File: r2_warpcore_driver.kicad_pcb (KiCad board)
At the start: 4 copper layers, 151 x 94.4 mm, 56 parts, among them J1 Conn_01x04_Pin, J10 Screw_Terminal_01x02, J11 Conn_01x03_Pin, J13 Conn_01x14_Pin, J14 Conn_01x05_Pin, J15 Conn_01x03_Pin, J16 Conn_01x03_Pin, J2 Conn_01x03_Pin, J3 Conn_01x03_Pin, J4 Conn_01x04_Pin, J5 Screw_Terminal_01x04, J6 Conn_01x05_Pin, J7 Screw_Terminal_01x04, J8 Screw_Terminal_01x04, J9 Screw_Terminal_01x03, Q1 L8050QLT1G, Q2 L8050QLT1G, Q3 IRLB8721PBF, Q4 IRLB8721PBF, Q5 IRLB8721PBF, Q6 Q_PNP_BEC, Q7 Q_PNP_BEC, Q8 Q_PNP_BEC, SW1 SW_Push, SW2 SW_Push, U1 ESP32-S3-MINI-1, U2 LDL1117S33R

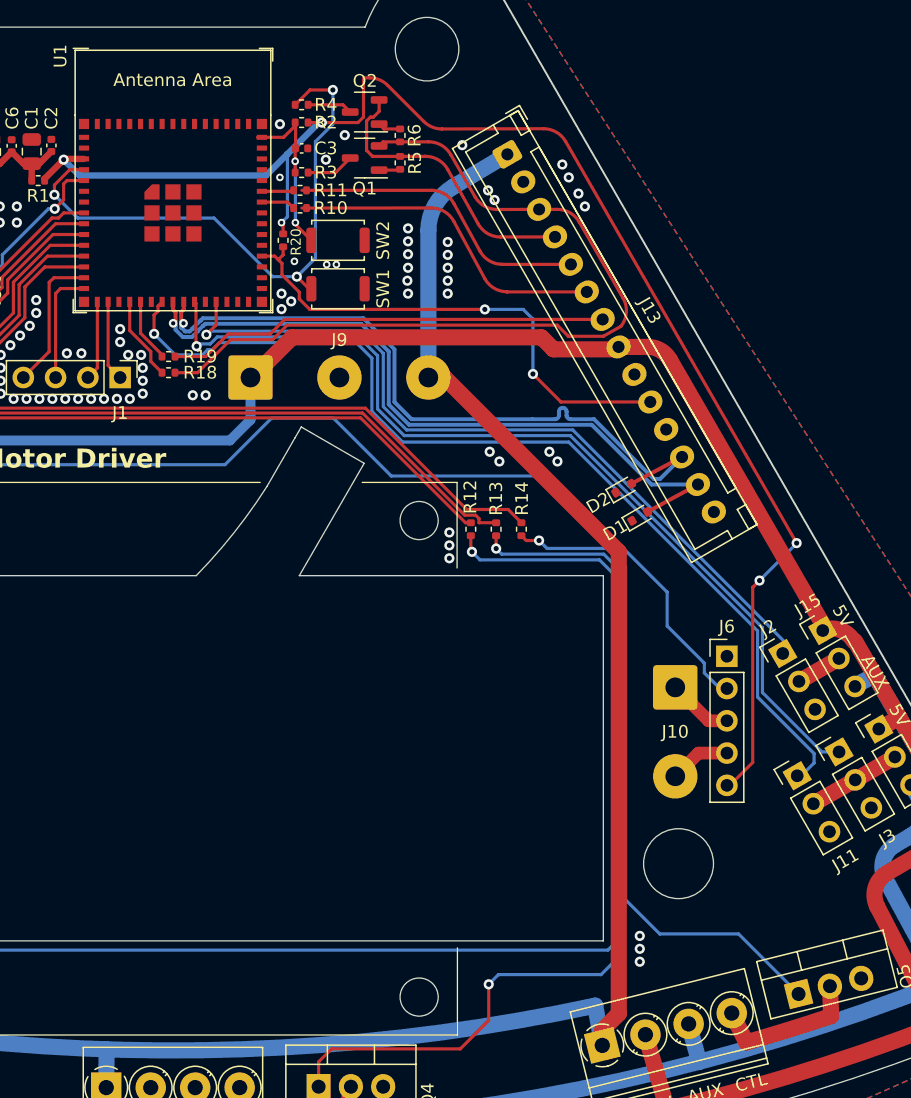
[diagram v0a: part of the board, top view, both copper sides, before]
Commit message: Updates to move to a USB socket.
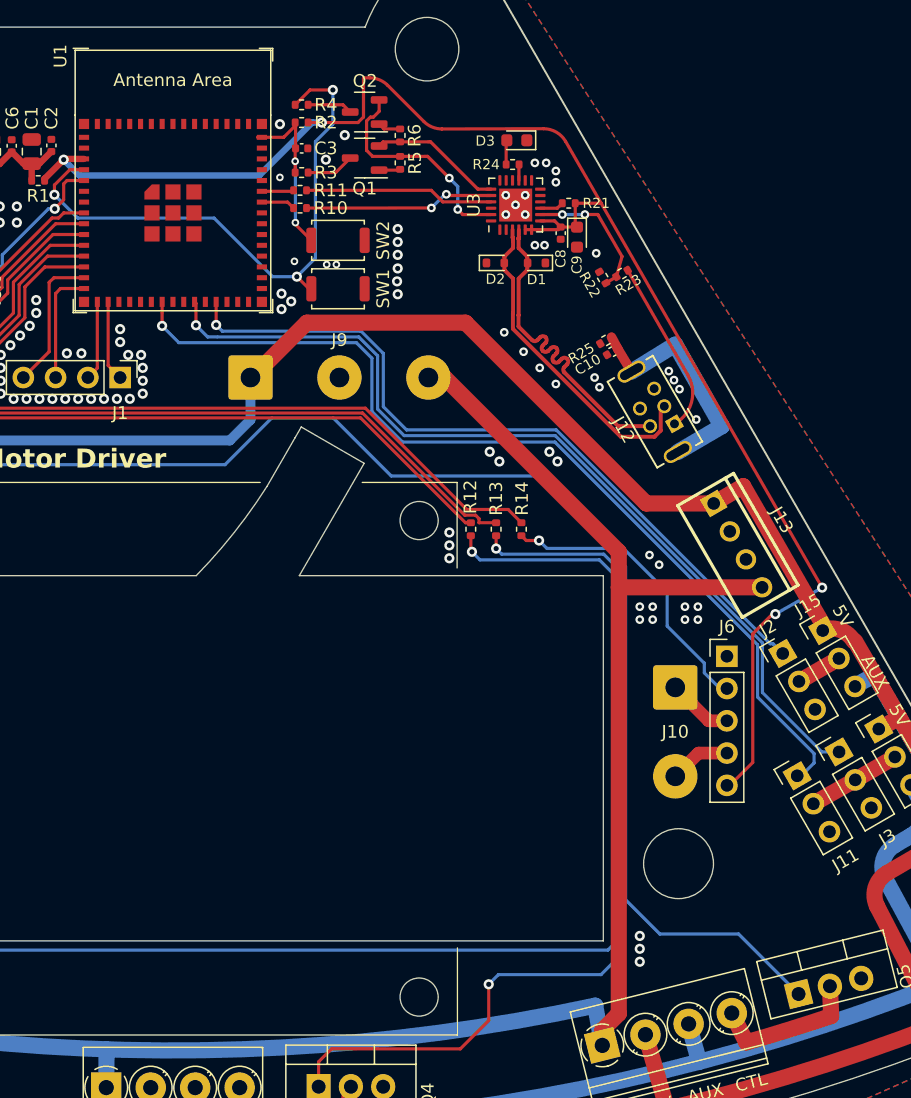
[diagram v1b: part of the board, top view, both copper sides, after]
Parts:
- removed R18, R19: 0(1%), Resistor_SMD:R_0402_1005Metric
- removed R20: 1K(1%), Resistor_SMD:R_0402_1005Metric
- added C10: 100nF, Capacitor_SMD:C_0402_1005Metric, F.Cu at (192.4, 69.3)
- added C8: 0.1uF/50V(10%), Capacitor_SMD:C_0402_1005Metric, F.Cu at (188.3, 60.0)
- added C9: 4.7uF/16V(10%), LED_SMD:LED_0603_1608Metric, F.Cu at (189.6, 60.3)
- added D3: RED, LED_SMD:LED_0603_1608Metric, F.Cu at (184.9, 52.7)
- added J12: USB_B_Micro, Connector_USB:USB_Mini-B_Tensility_54-00023_Vertical, F.Cu at (197.3, 75.0)
- added R21: 1K(1%), Resistor_SMD:R_0402_1005Metric, F.Cu at (189.0, 57.7)
- added R22: 47K, Resistor_SMD:R_0402_1005Metric, F.Cu at (191.6, 63.5)
- added R23: 22K, Resistor_SMD:R_0402_1005Metric, F.Cu at (193.2, 63.2)
- added R24: 220R, Resistor_SMD:R_0402_1005Metric, F.Cu at (184.6, 54.6)
- added R25: 330, Resistor_SMD:R_0402_1005Metric, F.Cu at (191.9, 68.5)
- added U3: CP2102N-Axx-xQFN24, Package_DFN_QFN:QFN-24-1EP_4x4mm_P0.5mm_EP2.6x2.6mm, F.Cu at (184.8, 57.8)
- J13: value Conn_01x14_Pin -> 171825-4; footprint Connector_JST:JST_XH_B14B-XH-A_1x14_P2.50mm_Vertical -> easyeda2kicad:HDR-TH_4P-P2.54-D1.0
- moved J13 35.7 mm to (202.3, 84.6)
- moved D1 21.5 mm to (186.4, 62.4), turned to 180 degrees
- moved D2 20.4 mm to (183.2, 62.4), turned to 0 degrees
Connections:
- net /ESP_3V3 renamed ESP_3V3
- net /VREG_EN renamed /power/VREG_EN
- D1 pad 2: /D- -> /usb/USB_N
- D2 pad 2: /D+ -> /usb/USB_P
- J13 pad 1: +12V -> +5V
- J13 pad 3: /RTS -> GND
- J13 pad 4: /DTR -> +12V
- Q1 pad 2: /RTS -> RTS
- Q2 pad 2: /DTR -> DTR
- R10 pad 2: /TXD -> USB_UART_RXD
- R11 pad 2: /RXD -> USB_UART_TXD
- R5 pad 1: /DTR -> DTR
- R6 pad 1: /RTS -> RTS
- U1 pad 19: /ESP_RTS -> unconnected-(U1-GPIO15/U0RTS/ADC2_CH4/XTAL_32K_P-Pad19)
- U1 pad 20: /ESP_CTS -> unconnected-(U1-GPIO16/U0CTS/ADC2_CH5/XTAL_32K_N-Pad20)
- U1 pad 23: /D- -> unconnected-(U1-GPIO19/U1RTS/ADC2_CH8/CLK_OUT2/USB_D--Pad23)
- U1 pad 24: /D+ -> unconnected-(U1-GPIO20/U1CTS/ADC2_CH9/CLK_OUT1/USB_D+-Pad24)
- U1 pad 34: /ID -> unconnected-(U1-GPIO38/FSPIWP/SUBSPIWP-Pad34)
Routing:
- net /RTS: track 65.3 -> 0.00 mm
- net /D-: track 56.4 -> 0.00 mm, vias 1 -> 0
- net /D+: track 56.4 -> 0.00 mm, vias 1 -> 0
- net /ID: track 39.9 -> 0.00 mm, vias 2 -> 0
- net /CTS: track 34.9 -> 0.00 mm
- net /TXD: track 25.8 -> 0.00 mm
- net /usb/USB_P: track 0.00 -> 25.8 mm
- net /usb/USB_N: track 0.00 -> 25.6 mm
- net /RXD: track 24.1 -> 0.00 mm
- net /DTR: track 22.8 -> 0.00 mm
- net Net-(J12-Shield): track 0.00 -> 18.6 mm
- net DTR: track 0.00 -> 17.5 mm, vias 0 -> 2
- net USB_UART_RXD: track 0.00 -> 15.0 mm, vias 0 -> 2
- net USB_UART_TXD: track 0.00 -> 14.9 mm
- net VBUS: track 0.00 -> 13.8 mm
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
